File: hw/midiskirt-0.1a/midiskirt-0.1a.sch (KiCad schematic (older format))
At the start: 13 parts, among them J1 DIN-5, J2 DIN-5, J3 DIN-5, U1 MC6850, U2 C64-Exp-Port, U3 74LS30, U4 4049, U5 6N137

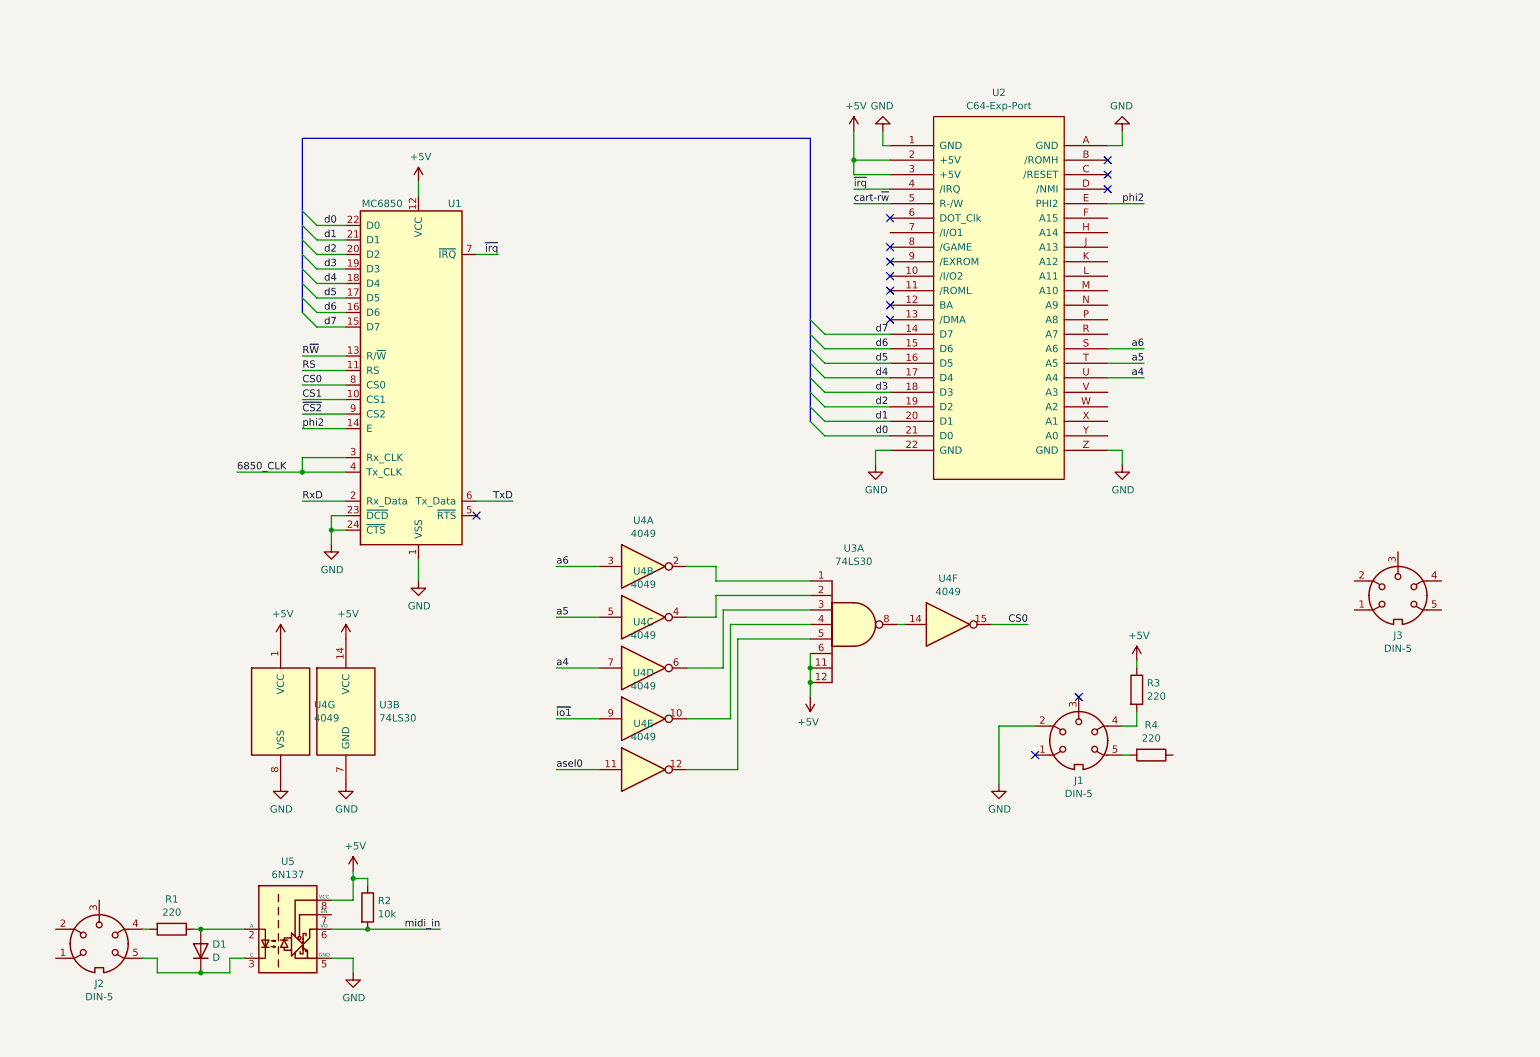
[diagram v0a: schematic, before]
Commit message: probably bad, stuck version w discrete dip logic
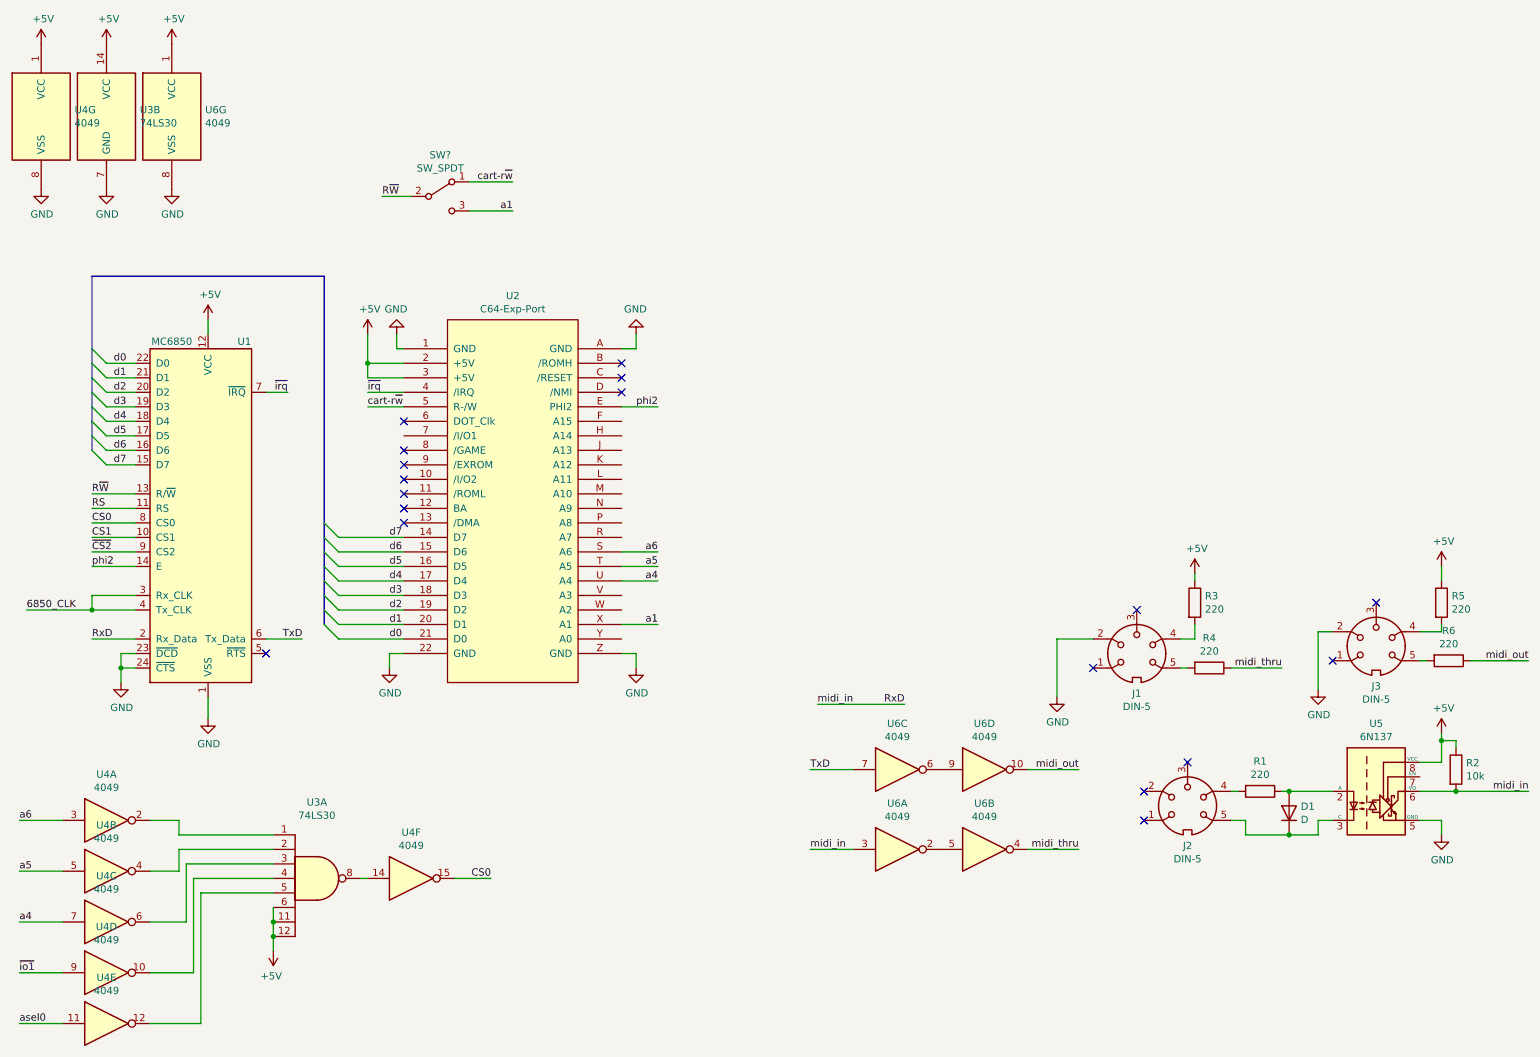
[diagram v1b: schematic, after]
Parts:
- added R5, R6: 220, Resistor_THT:R_Axial_DIN0207_L6.3mm_D2.5mm_P7.62mm_Horizontal, symbol Device:R
- added SW?: SW_SPDT, symbol Switch:SW_SPDT
- added U6: 4049, Package_DIP:DIP-16_W7.62mm, symbol 4xxx:4049
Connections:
- net midi_in is gone; now on net RxD: R2.2, U5.6 (VO)
- net +5V: now also R5.1, U6.1 (VCC)
- net GND: now also J3.2, U6.8 (VSS)
- net RxD: now also U6.3
- net R~W~: now also SW?.2 (B)
- net TxD: now also U6.7
- net cart-r~w~: now also SW?.1 (A)
- net a1: now reaches U2.X (A1)
- net a1: now also SW?.3 (C)
- net at J3.4: now also R5.2
- net at J3.5: now also R6.2
- net midi_thru: now reaches R4.1
- net midi_thru: now also U6.4
- new net: U6.2, U6.5
- new net: U6.6, U6.9
- new net midi_out: R6.1, U6.10
- no-connect marks 13 -> 18
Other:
- moved on the sheet: D1, J1, J2, J3, R1, R2, R3, R4, U1, U2, U3A, U3B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

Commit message: smt updates
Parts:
- removed SW?: SW_SPDT, symbol Switch:SW_SPDT
- removed U4, U6: 4049, Package_DIP:DIP-16_W7.62mm, symbol 4xxx:4049
- added U4: 74153, Package_SO:SOP-16_4.4x10.4mm_P1.27mm, symbol 74xx_IEEE:74153
- added U6: 74157, Package_SO:SOP-16_4.4x10.4mm_P1.27mm, symbol 74xx_IEEE:74157
- added U7: 4050, Package_SO:SOIC-16_4.55x10.3mm_P1.27mm, symbol 4xxx:4050
- added U8: SN74LVC1404, Package_SO:SSOP-8_2.95x2.8mm_P0.65mm, symbol midiskirt:SN74LVC1404
- added Y1: Crystal, Crystal:Crystal_HC49-U_Vertical, symbol Device:Crystal
- D1: footprint Diode_THT:D_T-1_P5.08mm_Horizontal -> Diode_SMD:D_SOD-123
- R1, R2, R3, R4, R5, R6: footprint Resistor_THT:R_Axial_DIN0207_L6.3mm_D2.5mm_P7.62mm_Horizontal -> Resistor_SMD:R_0603_1608Metric
- U3: footprint Package_DIP:DIP-14_W7.62mm -> Package_SO:SOIC-14_3.9x8.7mm_P1.27mm
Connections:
- net +5V: now also U4.16 (VCC), U6.16 (VCC), U7.1 (VCC), U8.8 (VCC); no longer U3.11, U3.12, U3.6
- net GND: now also U3.11, U3.12, U3.6, U4.1 (~ENa), U4.11 (I1b), U4.13 (I3b), U4.15 (~ENb), U4.5 (I1a), U4.8 (GND), U6.15 (~EN), U6.8 (GND), U7.8 (VSS), U8.4 (GND)
- net RxD: now also U7.6; no longer R2.2, U5.6 (VO)
- net R~W~: now also U6.7 (Qb)
- net TxD: now also U7.3
- net a1: now also U4.10 (I0b), U6.6 (I1b)
- net a4: now also U3.1
- net a5: now also U3.2
- net a6: now also U3.3
- net cart-r~w~: now also U6.5 (I0b)
- net midi_out: now also U7.2
- net midi_thru: now also U7.4
- net ~io1~: now also U2.7 (/I/O1), U3.4
- net a3: now reaches U2.V (A3)
- net a3: now also U4.6 (I0a), U6.3 (I1a)
- net a2: now reaches U2.W (A2)
- net a2: now also U4.12 (I2b), U4.3 (I3a), U6.2 (I0a)
- net at U3.5: now also U6.4 (Qa)
- net cs1: now reaches U3.8
- net cs1: now also U4.7 (Qa)
- new net: U8.2 (XOUT), Y1.1
- new net: U8.3 (XIN), Y1.2
- new net cs0: U4.4 (I2a)
- new net midi_in: R2.2, U5.6 (VO), U7.5, U7.7
- new net sel_a: U4.14 (A), U6.1 (A/B)
- new net sel_b: U4.2 (B)
- new net ~cs2~: U4.9 (Qb)

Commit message: first design that seems orderable
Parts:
- removed U6: 74157, Package_SO:SOP-16_4.4x10.4mm_P1.27mm, symbol 74xx_IEEE:74157
- removed U7: 4050, Package_SO:SOIC-16_4.55x10.3mm_P1.27mm, symbol 4xxx:4050
- removed U8: SN74LVC1404, Package_SO:SSOP-8_2.95x2.8mm_P0.65mm, symbol midiskirt:SN74LVC1404
- added C1, C2, C3, C4, C5, C6, C7: 0.1u, Capacitor_SMD:C_0603_1608Metric, symbol Device:C
- added SW1: SW_DP3T, midiskirt:C&K_JS203011CQN, symbol midiskirt:SW_DP3T
- added U2: 74LS393, Package_SO:SO-14_5.3x10.2mm_P1.27mm, symbol 74xx:74LS393
- added U3: 74LVC3G16, Package_SO:TSSOP-8_3x3mm_P0.65mm, symbol midiskirt:74LVC3G16
- added U7: SN74LVC1GX04, Package_TO_SOT_SMD:SOT-23-6_Handsoldering, symbol midiskirt:SN74LVC1GX04
- added U8: SN74LV4053A, Package_SO:SOIC-16_3.9x9.9mm_P1.27mm, symbol midiskirt:SN74LV4053A
- Y1: value Crystal -> 2 MHz; footprint Crystal:Crystal_HC49-U_Vertical -> Crystal:Crystal_HC49-4H_Vertical
- renumbered R3 to R1, R4 to R2, R1 to R3, R5 to R4, R6 to R5, R2 to R6, U3 to U1, U1 to U4, U4 to U5, U2 to U6, U5 to U9
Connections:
- net +5V: now also C1.1, C2.1, C3.1, C4.1, C5.1, C6.1, C7.1, SW1.2 (6), SW1.4 (8), SW1.8, U2.14 (VCC), U3.8 (VCC), U7.5 (VCC), U8.16 (VCC)
- net 6850_CLK: now also U8.15 (2Z)
- net GND: now also C1.2, C2.2, C3.2, C4.2, C5.2, C6.2, C7.2, SW1.1 (5), SW1.5, SW1.6, U2.2 (MR), U2.7 (GND), U3.4 (GND), U7.2 (GND), U8.6 (~EN~), U8.7 (VEE), U8.8 (GND)
- net RxD: now also U3.7
- net R~W~: now also U8.4 (3Z)
- net TxD: now also U3.6
- net a1: now also U8.3 (3Y1)
- net a2: now also U8.12 (1Y0)
- net a3: now also U8.13 (1Y1)
- net cart-r~w~: now also U8.5 (3Y0)
- net midi_in: now also U3.1, U3.3
- net midi_out: now also U3.2
- net midi_thru: now also U3.5
- net sel_a: now also SW1.3 (7), U8.10 (S2), U8.11 (S1)
- net sel_b: now also SW1.7, U8.9 (S3)
- net at Y1.1: now also U7.3 (X1)
- net at Y1.2: now also U7.4 (X2)
- net at U1.5: now also U8.14 (1Z)
- new net 2mhz: U2.1 (CP), U7.6 (Y), U8.1 (2Y1)
- new net 500khz: U2.4 (Q1), U8.2 (2Y0)
- no-connect marks 18 -> 21
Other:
- note added: "TODO: bias caps"
- moved on the sheet: U1B, Y1
